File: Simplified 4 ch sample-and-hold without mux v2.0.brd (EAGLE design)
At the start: 17.6 x 10 mm, 8 parts, among them IC5 TL074JT

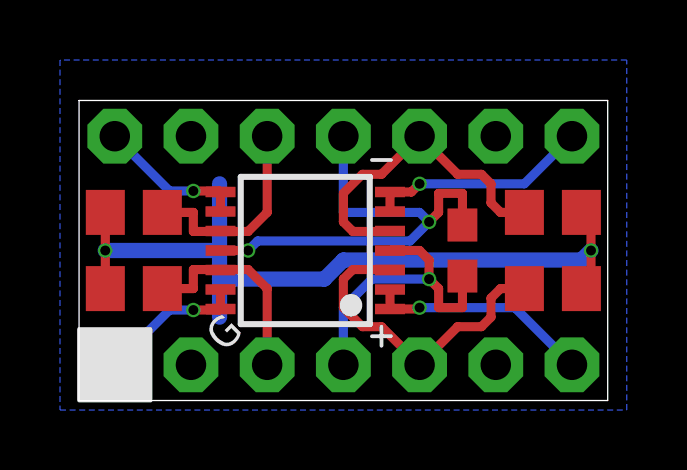
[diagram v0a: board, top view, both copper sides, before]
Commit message: changed from 0.1uF to 330pF to align with Fat Controller circuit
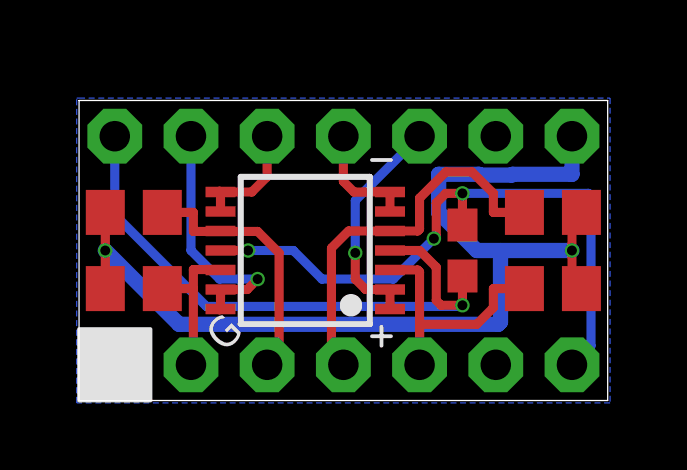
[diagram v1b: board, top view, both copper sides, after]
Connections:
- net +15V: now also 8-14.7; no longer 1-7.4
- net -15V: now also 1-7.7; no longer 8-14.4
- net AGND: now also 8-14.1; no longer 1-7.2
- net IN1: now also 1-7.2; no longer 1-7.3
- net IN2: now also 1-7.3, C27.2, IC5.10; no longer 1-7.5, C29.2, IC5.3
- net IN3: now also 1-7.4; no longer 8-14.3
- net IN4: now also 1-7.5, C29.2, IC5.3; no longer 8-14.5, C27.2, IC5.10
- net OUT1: now also 8-14.6; no longer 1-7.1
- net OUT2: now also 8-14.5, IC5.8, IC5.9; no longer 1-7.7, IC5.1, IC5.2
- net OUT3: now also 8-14.4; no longer 8-14.1
- net OUT4: now also 8-14.3, IC5.1, IC5.2; no longer 8-14.7, IC5.8, IC5.9
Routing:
- net +15V: track 10.2 -> 20.3 mm
- net AGND: track 26.4 -> 33.9 mm
- net -15V: track 15.8 -> 21.6 mm, vias 2 -> 3
- net OUT2: track 7.52 -> 3.81 mm, vias 1 -> 0
- net OUT3: track 7.49 -> 3.86 mm, vias 1 -> 0
- net OUT1: track 4.95 -> 8.51 mm
- net IN4: track 6.95 -> 9.79 mm
- net OUT4: track 4.95 -> 7.60 mm
- net IN3: track 10.9 -> 13.1 mm
- net IN2: track 10.9 -> 8.73 mm
- net IN1: track 6.95 -> 5.15 mm
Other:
- board text added: "S&H v2.0"
- board text removed: "S&H v1.0"

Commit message: Fixed error in silk screen
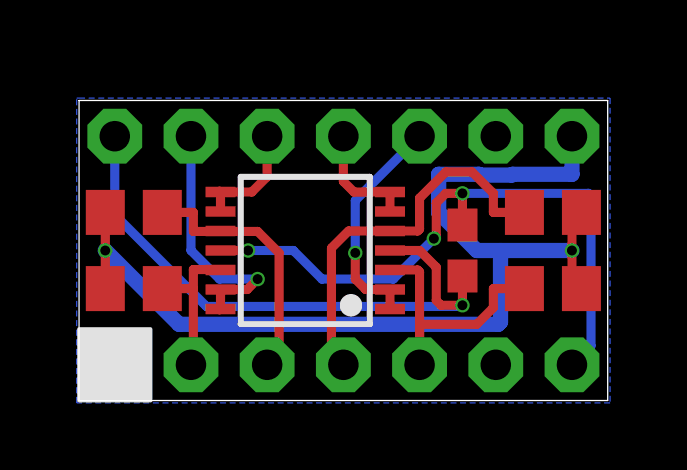
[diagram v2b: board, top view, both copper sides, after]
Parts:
- IC5: value TL074JT -> TL084CPWR
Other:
- board text added: "S&H v2.1"
- board text removed: "G"
- board text removed: "S&H v2.0"
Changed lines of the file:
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@@
 <?xml version="1.0" encoding="utf-8"?>
 <!DOCTYPE eagle SYSTEM "eagle.dtd">
-<eagle version="9.5.2">
+<eagle version="9.6.2">
 <drawing>
 <settings>
@@
 <layer number="23" name="tOrigins" color="15" fill="1" visible="no" active="yes"/>
 <layer number="24" name="bOrigins" color="15" fill="1" visible="yes" active="yes"/>
-<layer number="25" name="tNames" color="7" fill="1" visible="no" active="yes"/>
+<layer number="25" name="tNames" color="7" fill="1" visible="yes" active="yes"/>
 <layer number="26" name="bNames" color="7" fill="1" visible="yes" active="yes"/>
 <layer number="27" name="tValues" color="7" fill="1" visible="no" active="yes"/>
@@
 <wire x1="15.795625" y1="7.3025" x2="15.795625" y2="7.14375" width="0.127" layer="26"/>
 <text x="15.636875" y="3.730625" size="1.016" layer="26" font="vector" rot="MR0">S&amp;H
-v2.0</text>
+v2.1</text>
 <text x="1.905" y="3.254375" size="1.016" layer="26" font="vector" rot="MR90">4VOB</text>
 <polygon width="0.127" layer="25">
@@
 <vertex x="0" y="2.38125"/>
 </polygon>
-<wire x1="10.080625" y1="1.825625" x2="10.080625" y2="2.460625" width="0.127" layer="25"/>
-<wire x1="10.398125" y1="2.143125" x2="9.763125" y2="2.143125" width="0.127" layer="25"/>
-<wire x1="9.763125" y1="8.016875" x2="10.398125" y2="8.016875" width="0.127" layer="25"/>
-<text x="4.841875" y="1.5875" size="1.016" layer="25" font="vector" rot="R45">G</text>
 <polygon width="0.1524" layer="26">
 <vertex x="3.730625" y="7.62"/>
@@
 </autorouter>
 <elements>
-<element name="IC5" library="joakim" package="TSSOP14J" value="TL074JT" x="7.540625" y="5.000625" smashed="yes" rot="R90">
+<element name="IC5" library="joakim" package="TSSOP14J" value="TL084CPWR" x="7.540625" y="5.000625" smashed="yes" rot="R90">
 <attribute name="VALUE" x="9.445625" y="10.842625" size="1.27" layer="27" rot="R180"/>
 </element>
